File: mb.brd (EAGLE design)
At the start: 160 x 100 mm, 6 parts, among them J1 PJ-002BH-SMT-TR, U1 PEM1-S12-S5-S

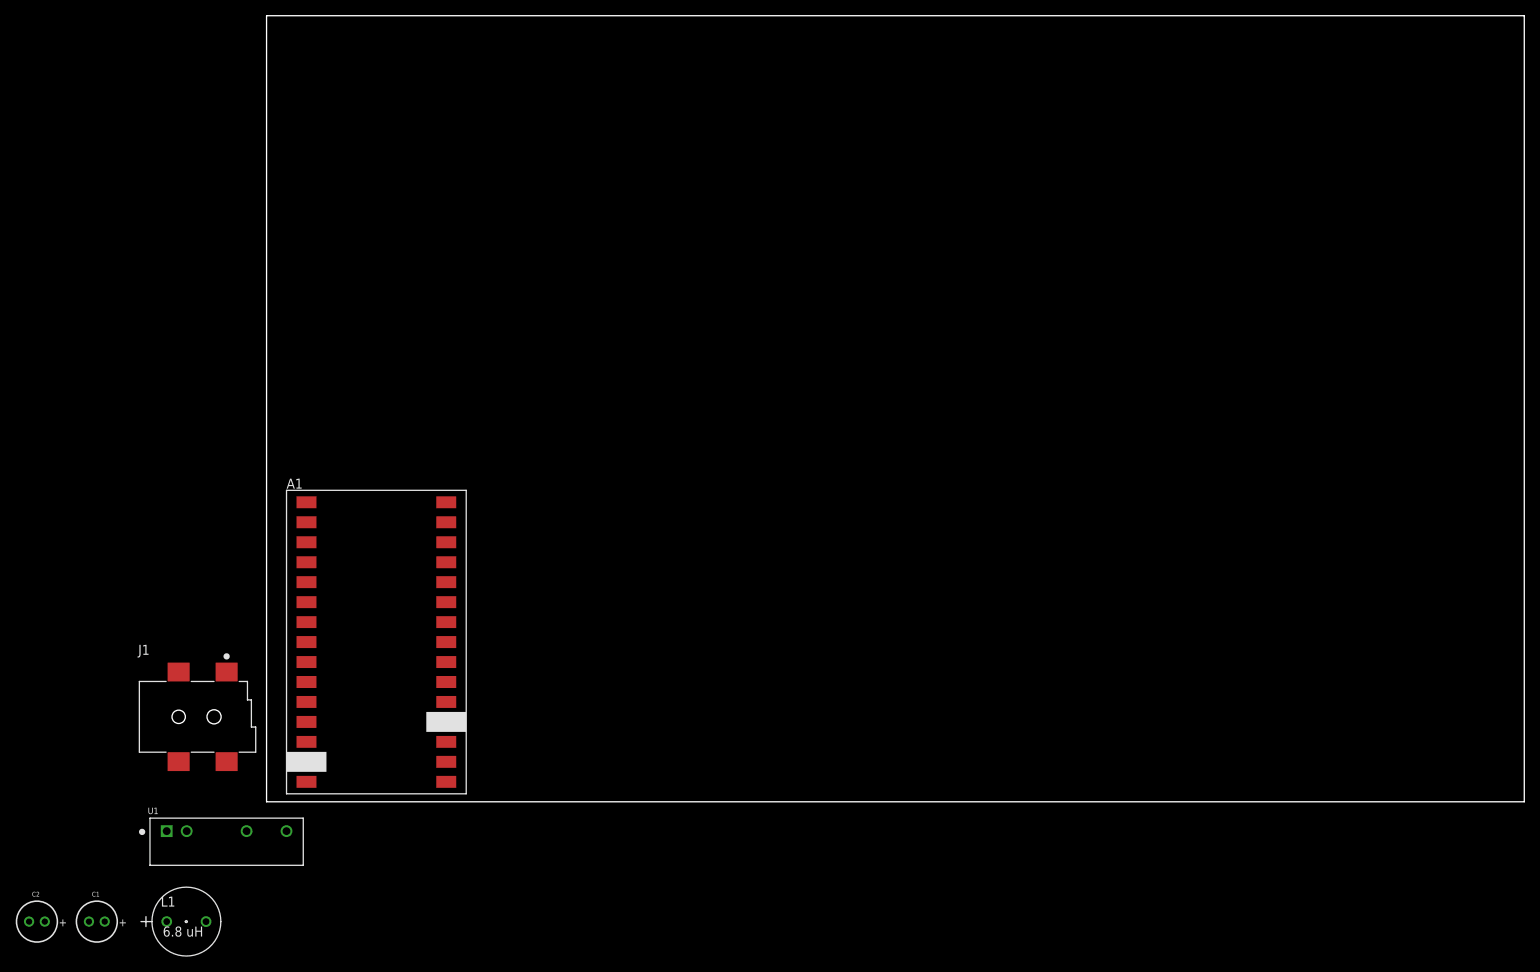
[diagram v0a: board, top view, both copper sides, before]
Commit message: Adding io components, level shifters
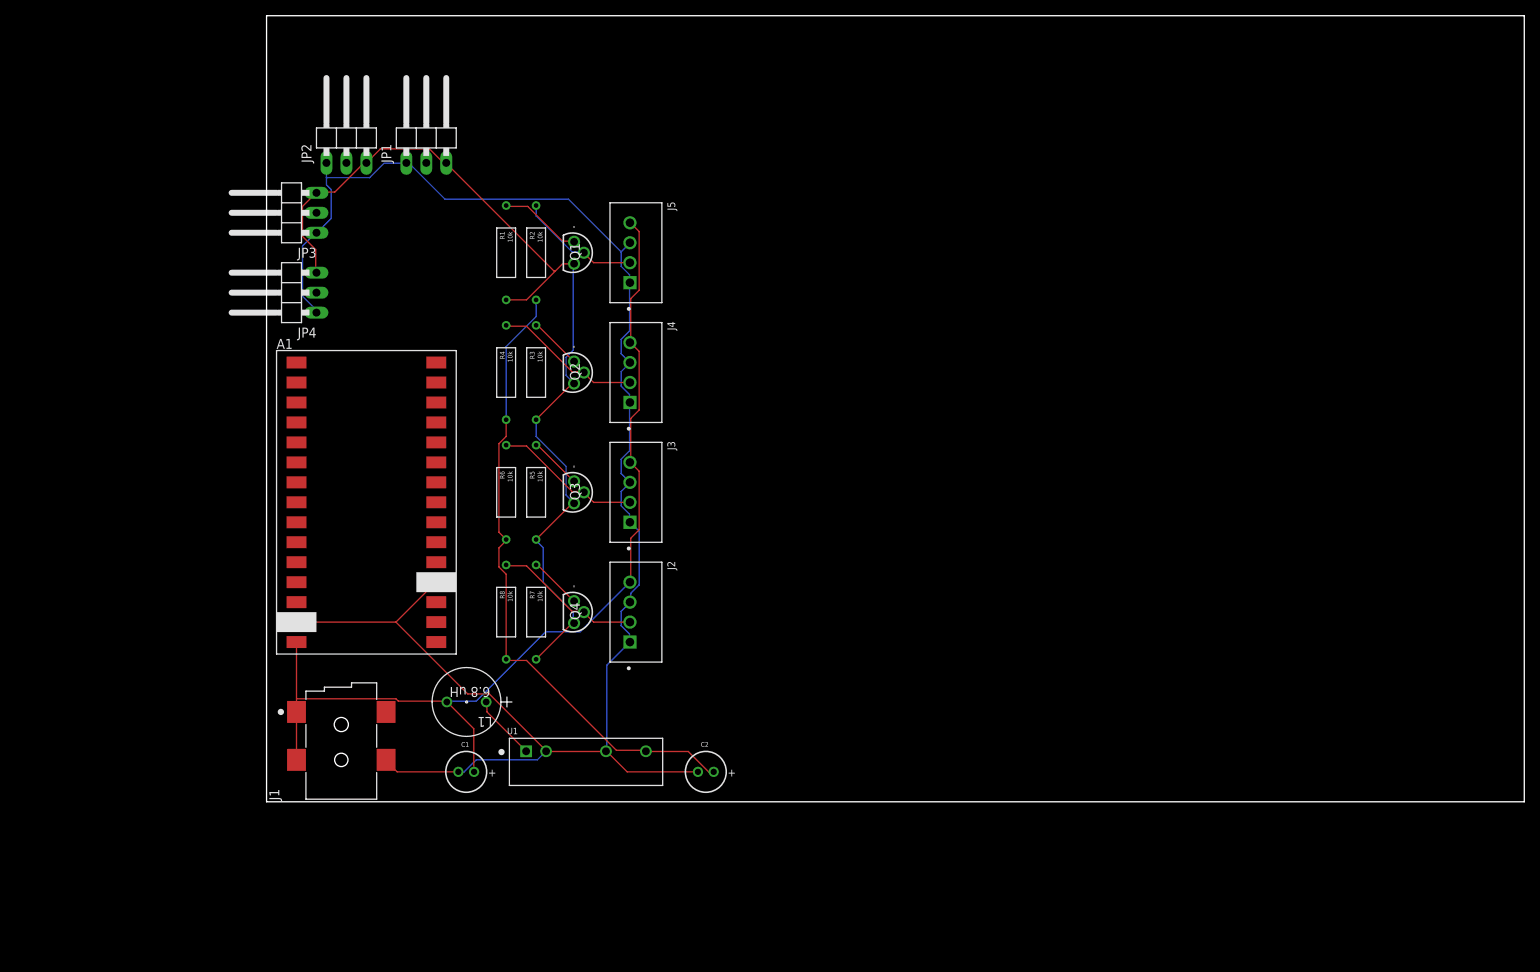
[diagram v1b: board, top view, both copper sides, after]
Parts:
- added J2, J3, J4, J5: MOLEX_70543-0003MOLEX_70543-0003_0_0, Molex - 70543-0003:MOLEX_70543-0003_0
- added JP1, JP2, JP3, JP4: (no value), pinhead:1X03/90
- added Q1, Q2, Q3, Q4: TN0702N3-G, SamacSys_Parts:LND150N3-G
- added R1, R2, R3, R4, R5, R6, R7, R8: 10k, ref_lib:CFR-25
- moved C2 87.2 mm to (55.9, 3.81)
- moved C1 50.7 mm to (25.4, 3.81)
- moved L1 49.3 mm to (27.9, 12.7), turned to 180 degrees
- moved U1 46.8 mm to (40.6, 5.08)
- moved A1 17.8 mm to (3.81, 55.9)
- moved J1 10.2 mm to (3.81, 11.4), turned to 90 degrees
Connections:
- new net +3.3V: JP1.3, JP2.3, JP3.3, JP4.3, Q1.3, Q2.3, Q3.3, Q4.3, R1.P$2, R3.P$2, R5.P$2, R7.P$2
- new net BOOL1: JP1.2
- new net BOOL2: JP2.2
- new net BOOL3: JP3.2
- new net BOOL4: JP4.2
- new net LC1: Q4.1, R7.P$1
- new net LC2: Q3.1, R5.P$1
- new net LC3: Q2.1, R3.P$1
- new net LC4: Q1.1, R1.P$1
- new net LED1: J2.2, Q4.2, R8.P$1
- new net LED2: J3.2, Q3.2, R6.P$1
- new net LED3: J4.2, Q2.2, R4.P$1
- new net LED4: J5.2, Q1.2, R2.P$1
- net +12V: now also J2.4, J3.4, J4.4, J5.4
- net +5V: now also R2.P$2, R4.P$2, R6.P$2, R8.P$2
- net GND: now also J2.1, J2.3, J3.1, J3.3, J4.1, J4.3, J5.1, J5.3, JP1.1, JP2.1, JP3.1, JP4.1
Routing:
- net GND: track 0.00 -> 225.4 mm
- net +3.3V: track 0.00 -> 123.4 mm
- net +12V: track 0.00 -> 122.9 mm
- net +5V: track 0.00 -> 81.2 mm
- net LED3: track 0.00 -> 18.8 mm
- net LED1: track 0.00 -> 18.8 mm
- net LED2: track 0.00 -> 18.8 mm
- net LED4: track 0.00 -> 15.7 mm
- net LC4: track 0.00 -> 10.6 mm
- net N$1: track 0.00 -> 8.39 mm
- net LC3: track 0.00 -> 6.79 mm
- net LC1: track 0.00 -> 6.79 mm
- net LC2: track 0.00 -> 6.79 mm

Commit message: Final Board layout with eeprom
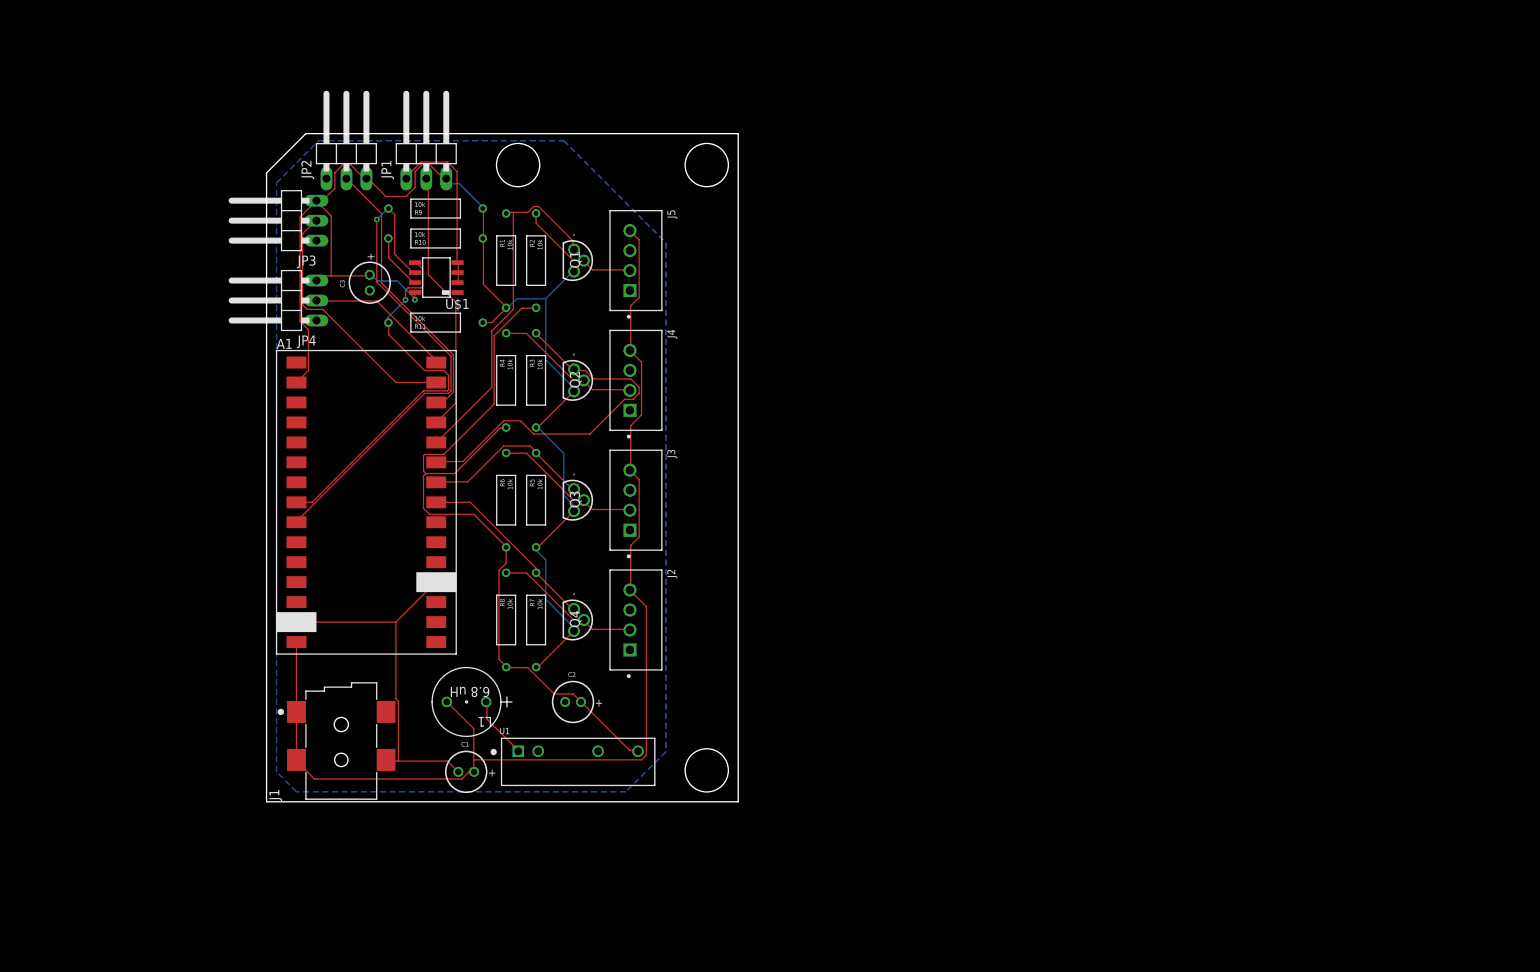
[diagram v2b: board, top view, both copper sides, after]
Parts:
- added C3: 0.1 µF, 860020672008_Eagle_WCAP-ATG5_rev20a:WCAP-ATG5_5X11(DXL)
- added R10, R11, R9: 10k, ref_lib:CFR-25
- added U$1: AT24CM01-SSHM-T, ref_lib:8-SOIC(3.9MM)
- moved C2 19.1 mm to (39.0, 12.7)
- moved JP1 2.00 mm to (20.3, 83.1)
- moved JP2 2.00 mm to (10.2, 83.1)
- moved J2 1.00 mm to (47.0, 23.1)
- moved J3 1.00 mm to (47.0, 38.4)
- moved J4 1.00 mm to (47.0, 53.6)
- moved J5 1.00 mm to (47.0, 68.8)
- moved JP3 1.00 mm to (2.54, 73.9)
- moved Q1 1.00 mm to (39.4, 68.8)
- moved Q2 1.00 mm to (39.4, 53.6)
- moved Q3 1.00 mm to (39.4, 38.4)
- moved Q4 1.00 mm to (39.4, 23.1)
- moved R1 1.00 mm to (30.5, 68.8)
- moved R2 1.00 mm to (34.3, 68.8)
- moved R3 1.00 mm to (34.3, 53.6)
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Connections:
- new net SCL: A1.A5, R9.P$1, U$1.P5
- new net SDA: A1.A4, R11.P$1, U$1.P4
- new net WP: R10.P$1, U$1.P6
- net +3.3V: now also A1.+3.3V, C3.1, R10.P$2, R11.P$2, R9.P$2, U$1.P7
- net BOOL1: now also A1.D9
- net BOOL2: now also A1.D10
- net BOOL3: now also A1.D11
- net BOOL4: now also A1.D12
- net GND: now also C3.2, U$1.P1, U$1.P2, U$1.P3
- net LC1: now also A1.D5
- net LC2: now also A1.D6
- net LC3: now also A1.D7
- net LC4: now also A1.D8
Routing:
- net GND: track 225.4 -> 69.9 mm
- net SCL: track 0.00 -> 64.1 mm, vias 0 -> 1
- net SDA: track 0.00 -> 49.6 mm, vias 0 -> 1
- net +3.3V: track 123.4 -> 170.8 mm, vias 0 -> 1
- net LC3: track 6.79 -> 47.8 mm
- net BOOL2: track 0.00 -> 35.6 mm
- net LC4: track 10.6 -> 45.3 mm
- net BOOL1: track 0.00 -> 33.6 mm
- net BOOL3: track 0.00 -> 32.6 mm
- net +12V: track 122.9 -> 142.4 mm
- net BOOL4: track 0.00 -> 18.7 mm
- net LC1: track 6.79 -> 23.6 mm
- net +5V: track 81.2 -> 96.8 mm
- net LC2: track 6.79 -> 21.9 mm
- net WP: track 0.00 -> 7.19 mm
- added copper zone on layer 16, net GND
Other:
- board size 160 x 100 mm -> 60 x 85 mm

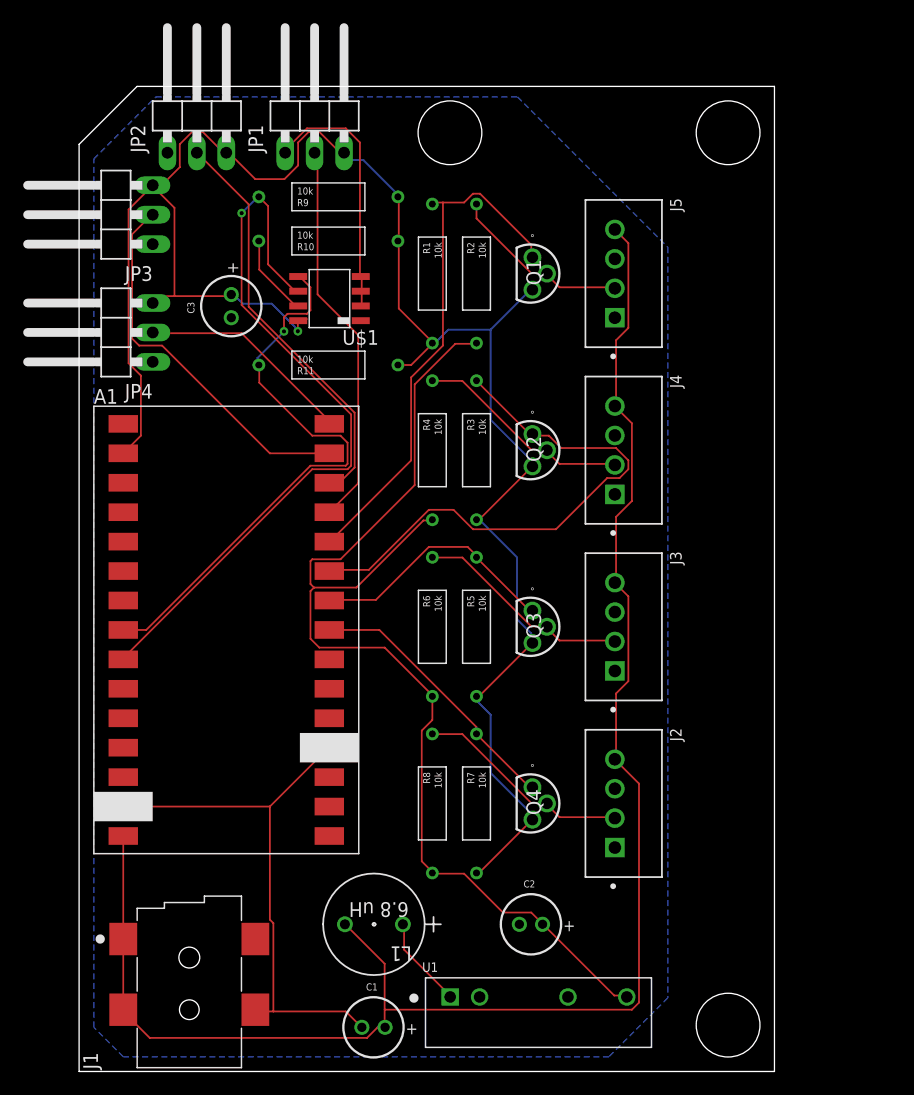
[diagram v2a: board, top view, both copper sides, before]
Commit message: Finish 1st layout. Add cam profile
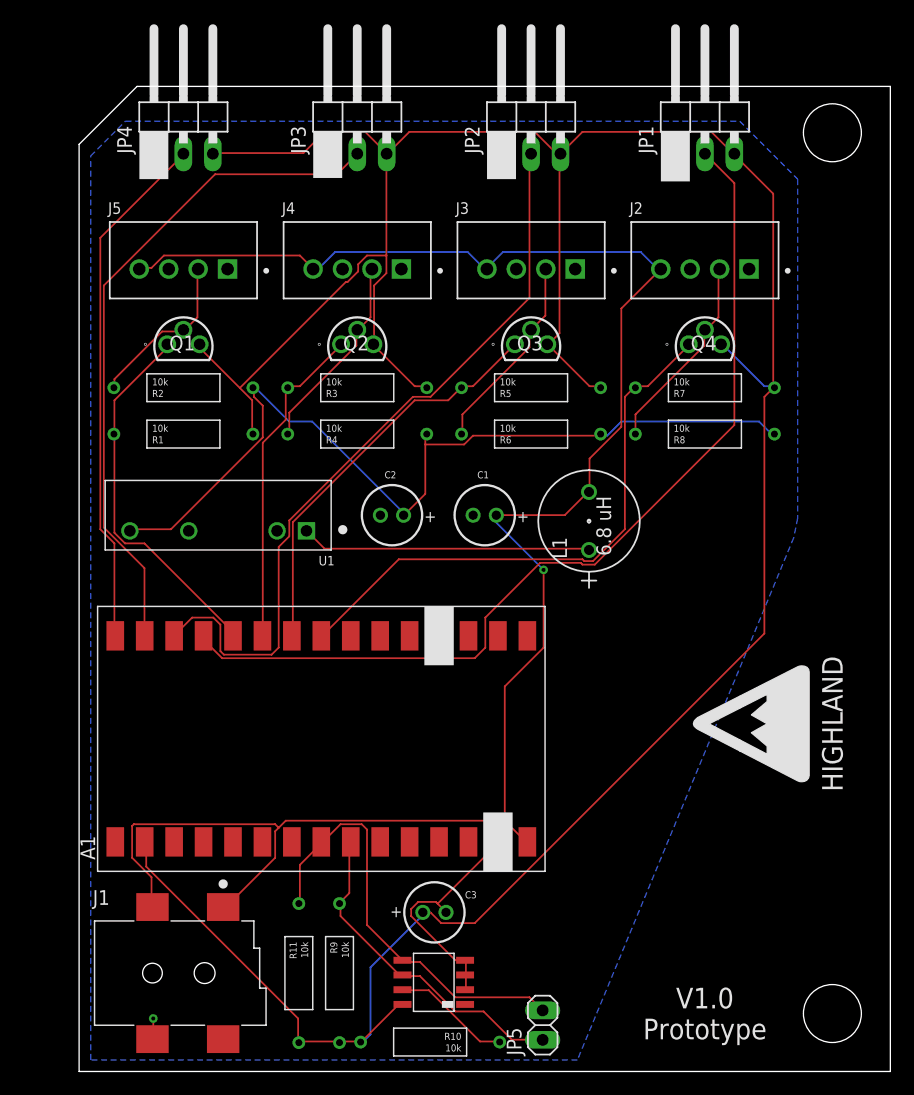
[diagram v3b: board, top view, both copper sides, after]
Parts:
- added JP5: (no value), pinhead:1X02
- moved R10 69.7 mm to (30.3, 2.54), turned to 180 degrees
- moved R9 67.0 mm to (22.5, 8.49), turned to 270 degrees
- moved U$1 59.7 mm to (33.3, 5.79)
- moved C3 55.2 mm to (30.7, 13.7), turned to 180 degrees
- moved R11 52.5 mm to (19.0, 8.49), turned to 270 degrees
- moved U1 51.0 mm to (12.0, 48.0), turned to 180 degrees
- moved J2 47.4 mm to (54.0, 70.0), turned to 0 degrees
- moved C1 45.2 mm to (35.0, 48.0)
- moved Q4 42.5 mm to (54.0, 63.0), turned to 0 degrees
- moved R7 40.9 mm to (54.0, 59.0), turned to 0 degrees
- moved R8 39.6 mm to (54.0, 55.0), turned to 0 degrees
- moved J5 38.0 mm to (9.00, 70.0), turned to 0 degrees
- moved C2 37.3 mm to (27.0, 48.0)
- moved A1 36.1 mm to (3.12, 19.8), turned to 90 degrees
- moved L1 36.1 mm to (44.0, 45.0), turned to 90 degrees
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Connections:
- net SCL: now also JP5.1
- net SDA: now also JP5.2
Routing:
- net +3.3V: track 170.8 -> 260.0 mm, vias 1 -> 0
- net BOOL1: track 33.6 -> 81.2 mm
- net GND: track 69.9 -> 24.3 mm, vias 0 -> 2
- net SCL: track 64.1 -> 28.7 mm, vias 1 -> 0
- net BOOL2: track 35.6 -> 65.1 mm
- net BOOL4: track 18.7 -> 45.1 mm
- net BOOL3: track 32.6 -> 58.3 mm
- net LC1: track 23.6 -> 49.0 mm
- net +5V: track 96.8 -> 76.7 mm
- net LC3: track 47.8 -> 28.5 mm
- net +12V: track 142.4 -> 160.6 mm, vias 0 -> 1
- net N$1: track 7.98 -> 25.1 mm
- net LC2: track 21.9 -> 35.4 mm
- net LC4: track 45.3 -> 32.3 mm
- net SDA: track 49.6 -> 37.3 mm, vias 1 -> 0
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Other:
- board size 60 x 85 mm -> 70 x 85 mm
- board text added: "HIGHLAND"
- board text added: "V1.0 Prototype"

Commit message: Finalized v1.0 prototype
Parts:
- added R12: 270, ref_lib:CFR-25
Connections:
- net +3.3V: no longer R10.P$2
- net +5V: now also R12.P$2
- net GND: now also R10.P$2, R12.P$1
- net WP: now also A1.A6
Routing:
- net +12V: track 160.6 -> 177.6 mm, vias 1 -> 6
- net WP: track 10.3 -> 24.3 mm
- net SDA: track 37.3 -> 51.1 mm
- net BOOL2: track 65.1 -> 54.4 mm, vias 0 -> 1
- net +5V: track 76.7 -> 82.7 mm, vias 0 -> 1
- net LC2: track 35.4 -> 41.2 mm
- net GND: track 24.3 -> 18.9 mm
- net +3.3V: track 260.0 -> 264.8 mm
- net BOOL3: track 58.3 -> 53.5 mm, vias 0 -> 2
- net SCL: track 28.7 -> 32.1 mm
- net LC1: track 49.0 -> 51.2 mm
- net BOOL1: track 81.2 -> 82.7 mm
- net LC4: track 32.3 -> 33.2 mm
- net LED4: track 14.4 -> 15.2 mm
- net BOOL4: vias 0 -> 2

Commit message: First built boards
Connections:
- net +3.3V: now also R10.P$2
- net GND: no longer R10.P$2
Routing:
- net +3.3V: track 264.8 -> 266.0 mm
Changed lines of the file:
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@@
 <contactref element="U$1" pad="P2"/>
 <contactref element="U$1" pad="P3"/>
-<contactref element="R10" pad="P$2"/>
 <contactref element="R12" pad="P$1"/>
 <wire x1="33.2994" y1="8.3058" x2="33.2994" y2="7.0866" width="0.1524" layer="1"/>
@@
 <contactref element="C3" pad="1"/>
 <wire x1="25.6794" y1="5.715" x2="27.8892" y2="5.715" width="0.1524" layer="1"/>
-<wire x1="22.479" y1="2.5146" x2="25.6794" y2="5.715" width="0.1524" layer="1"/>
+<wire x1="22.479" y1="2.5146" x2="23.3934" y2="3.429" width="0.1524" layer="1"/>
+<wire x1="23.3934" y1="3.429" x2="25.6794" y2="5.715" width="0.1524" layer="1"/>
 <wire x1="27.8892" y1="5.715" x2="27.904" y2="5.786" width="0.1524" layer="1"/>
 <wire x1="22.479" y1="2.5146" x2="22.47" y2="2.49" width="0.1524" layer="1"/>
@@
 <wire x1="5.6388" y1="19.812" x2="5.66" y2="19.81" width="0.1524" layer="1"/>
 <wire x1="11.5062" y1="79.1718" x2="11.54" y2="79.19" width="0.1524" layer="1"/>
+<contactref element="R10" pad="P$2"/>
+<wire x1="23.3934" y1="3.429" x2="24.2316" y2="2.5908" width="0.1524" layer="1"/>
+<wire x1="24.2316" y1="2.5908" x2="24.29" y2="2.54" width="0.1524" layer="1"/>
 </signal>
 <signal name="LC4">
